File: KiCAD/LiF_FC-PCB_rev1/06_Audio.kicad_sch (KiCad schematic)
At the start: 0 parts

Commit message: fixed my schematics syncing (I think), and added accelorometer schematic. Pushing since I need to switch main.
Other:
- company: (none) -> Conestoga College
- title: (none) -> LiF - PD, UI, and Audio
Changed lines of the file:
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@@
 	(generator_version "9.0")
 	(paper "A4")
+	(title_block
+		(title "LiF - PD, UI, and Audio")
+		(date "2026-07-02")
+		(rev "0")
+		(company "Conestoga College")
+		(comment 1 "Designed by NK")
+	)
 )

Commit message: updated schematics and pushing so MR can pull and begin merge.
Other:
- note added: "WIP"
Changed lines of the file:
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@@
 		(comment 1 "Designed by NK")
 	)
+	(text "WIP"
+		(exclude_from_sim no)
+		(at 168.656 71.12 0)
+		(effects
+			(font
+				(size 1.27 1.27)
+			)
+			(justify left)
+		)
+	)
 )

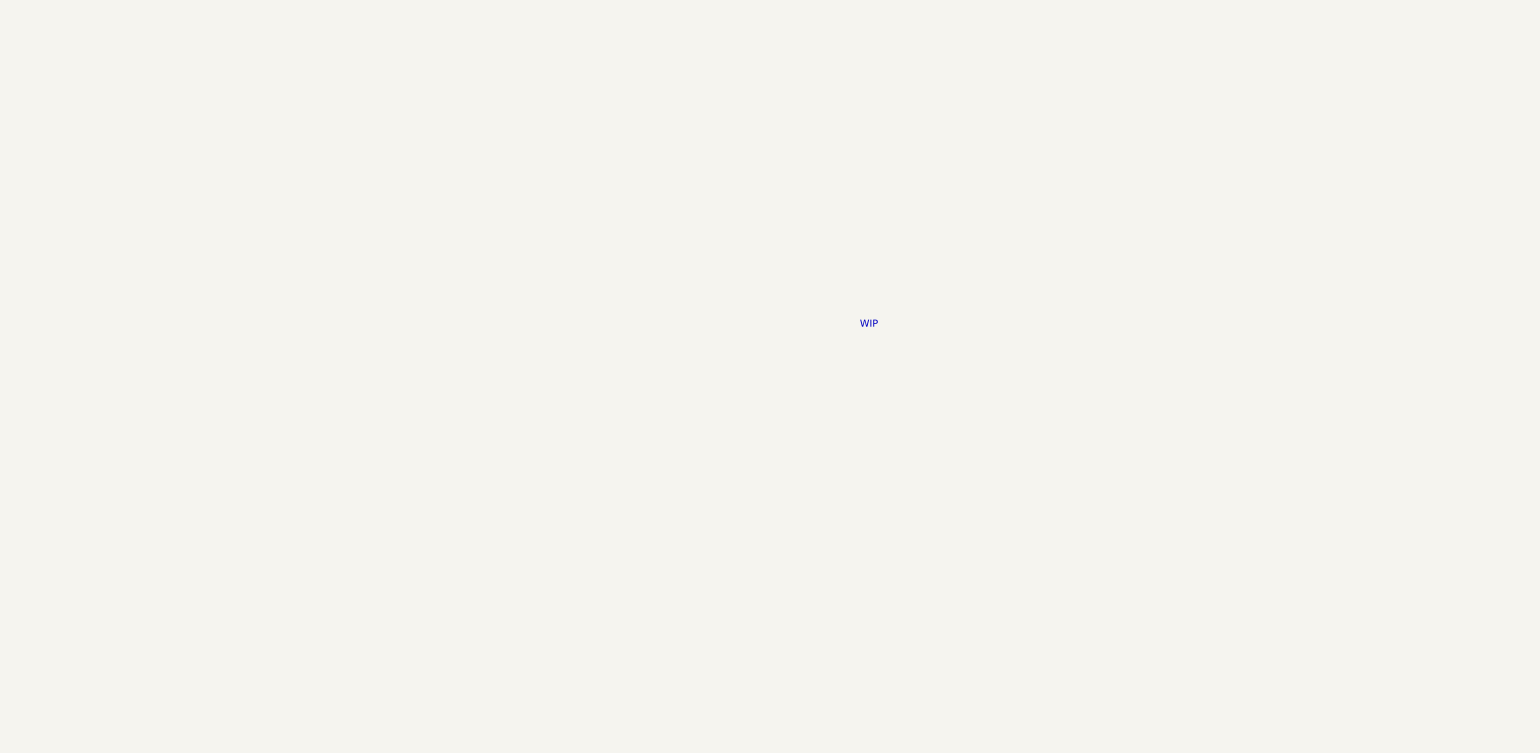
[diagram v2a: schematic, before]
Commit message: added RY's PHP (she provided a zip file so I pasted the code over) and added the audio schmematic
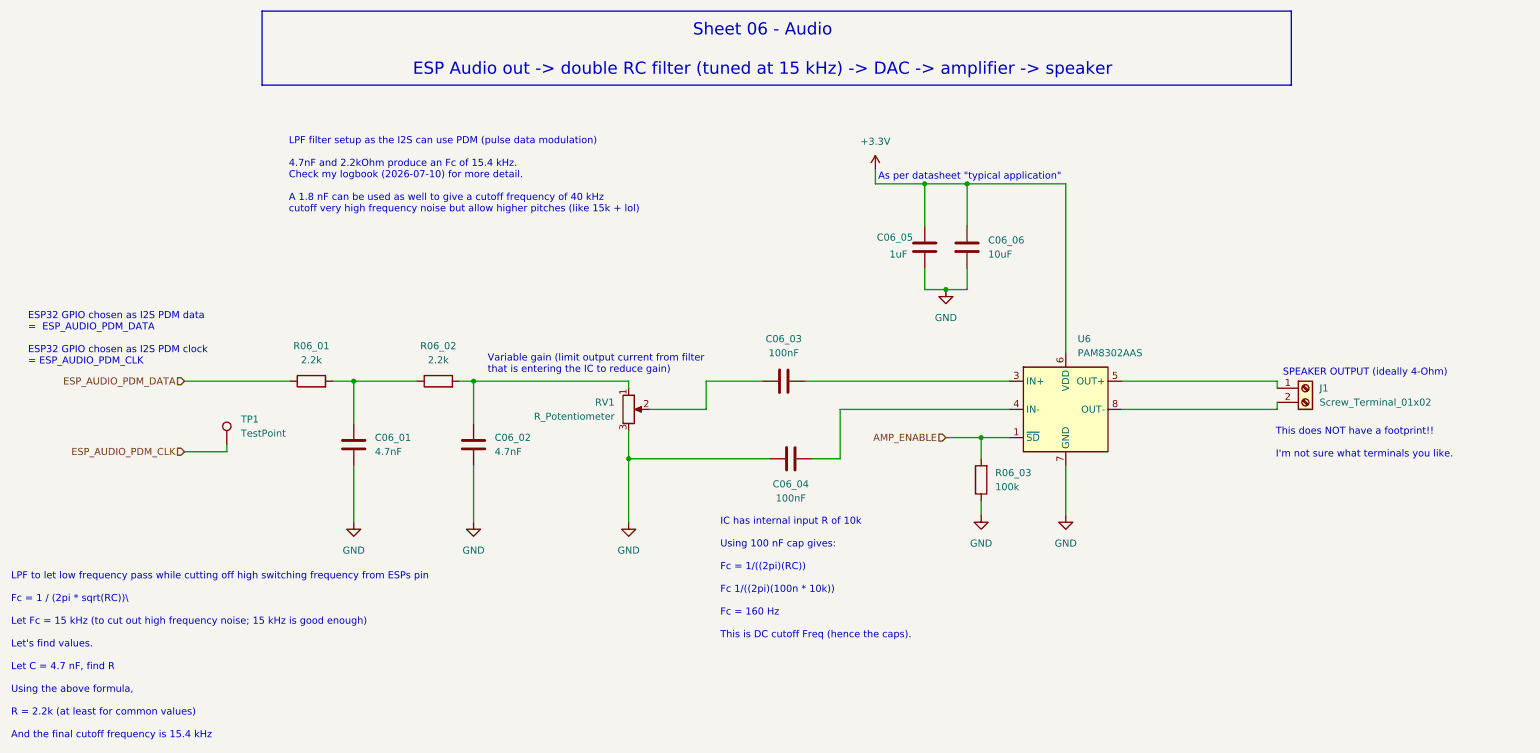
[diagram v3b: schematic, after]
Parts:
- added C06_01, C06_02: 4.7nF, symbol Device:C
- added C06_03, C06_04: 100nF, symbol Device:C
- added C06_05: 1uF, symbol Device:C
- added C06_06: 10uF, symbol Device:C
- added J1: Screw_Terminal_01x02, symbol Connector:Screw_Terminal_01x02
- added R06_01, R06_02: 2.2k, symbol Device:R
- added R06_03: 100k, symbol Device:R
- added RV1: R_Potentiometer, symbol Device:R_Potentiometer
- added TP1: TestPoint, TestPoint:TestPoint_Bridge_Pitch2.54mm_Drill1.0mm, symbol Connector:TestPoint
- added U6: PAM8302AAS, Package_SO:MSOP-8_3x3mm_P0.65mm, symbol Amplifier_Audio:PAM8302AAS
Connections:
- new net: C06_01.1, R06_01.2, R06_02.1
- new net: C06_03.1, RV1.2
- new net: C06_03.2, U6.3 (IN+)
- new net: J1.1 (Pin_1), U6.5 (OUT+)
- new net: J1.2 (Pin_2), U6.8 (OUT-)
- new net: C06_02.1, R06_02.2, RV1.1
- new net: C06_04.2, U6.4 (IN-)
- new net +3.3V: C06_05.1, C06_06.1, U6.6 (VDD)
- new net AMP_ENABLE: R06_03.2, U6.1 (~{SD})
- new net ESP_AUDIO_PDM_CLK: TP1.1
- new net ESP_AUDIO_PDM_DATA: R06_01.1
- new net GND: C06_01.2, C06_02.2, C06_04.1, C06_05.2, C06_06.2, R06_03.1, RV1.3, U6.7 (GND)
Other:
- note added: "As per datasheet "typical application""
- note added: "ESP32 GPIO chosen as I2S PDM data = ESP_AUDIO_PDM_DATA ESP32 GPIO chosen as I2S PDM clock = ESP_AUDIO_PDM_CLK"
- note added: "IC has internal input R of 10k Using 100 nF cap gives: Fc = 1/((2pi)(RC)) Fc 1/((2pi)(100n * 10k)) Fc = 160 Hz This is DC cutoff Freq (hence the caps)."
- note added: "LPF filter setup as the I2S can use PDM (pulse data modulation) 4.7nF and 2.2kOhm produce an Fc of 15.4 kHz. Check my logbook (2026-07-10) for more detail. A 1.8 nF can be used as well to give a cutoff frequency of 40 kHz cutoff very high frequency noise but allow higher pitches (like 15k + lol)"
- note added: "LPF to let low frequency pass while cutting off high switching frequency from ESPs pin Fc = 1 / (2pi * sqrt(RC))\ Let Fc = 15 kHz (to cut out high frequency noise; 15 kHz is good enough) Let's find values. Let C = 4.7 nF, find R Using the above formula, R = 2.2k (at least for common values) And the final cutoff frequency is 15.4 kHz"
- note added: "SPEAKER OUTPUT (ideally 4-Ohm)"
- note added: "Sheet 06 - Audio ESP Audio out -> double RC filter (tuned at 15 kHz) -> DAC -> amplifier -> speaker"
- note added: "This does NOT have a footprint!! I'm not sure what terminals you like."
- note added: "Variable gain (limit output current from filter that is entering the IC to reduce gain)"
- note removed: "WIP"
